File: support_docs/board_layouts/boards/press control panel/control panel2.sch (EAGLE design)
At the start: 21 parts, among them X1 009176002

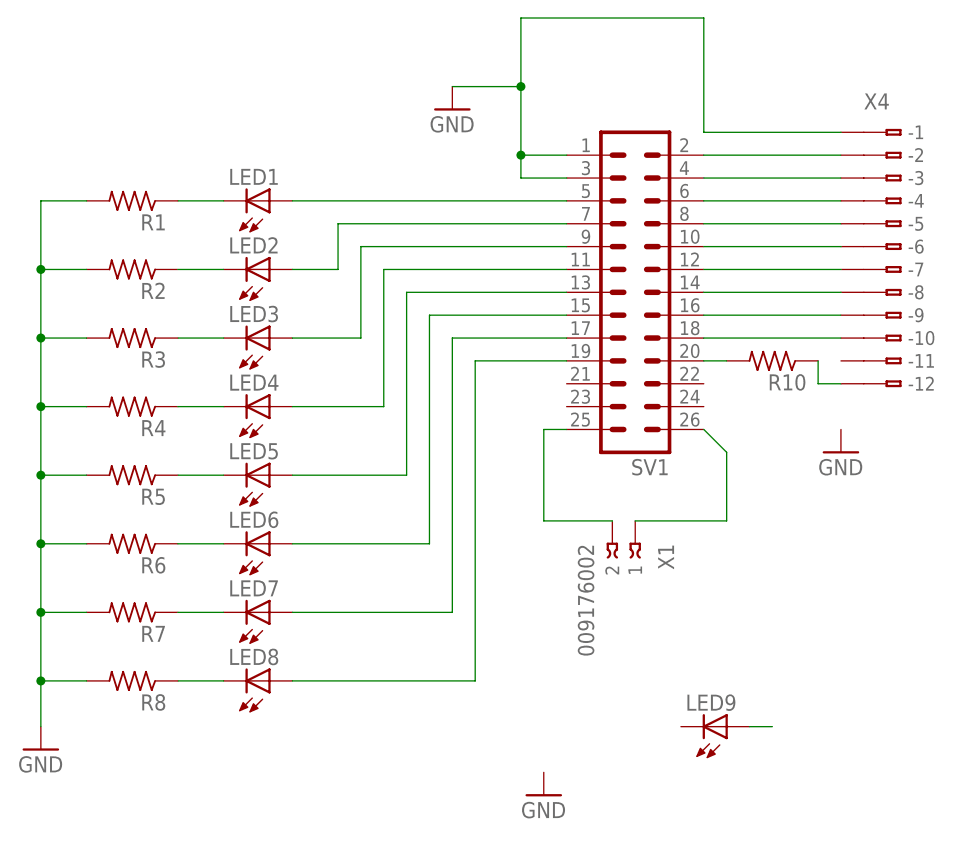
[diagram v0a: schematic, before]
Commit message: add led control
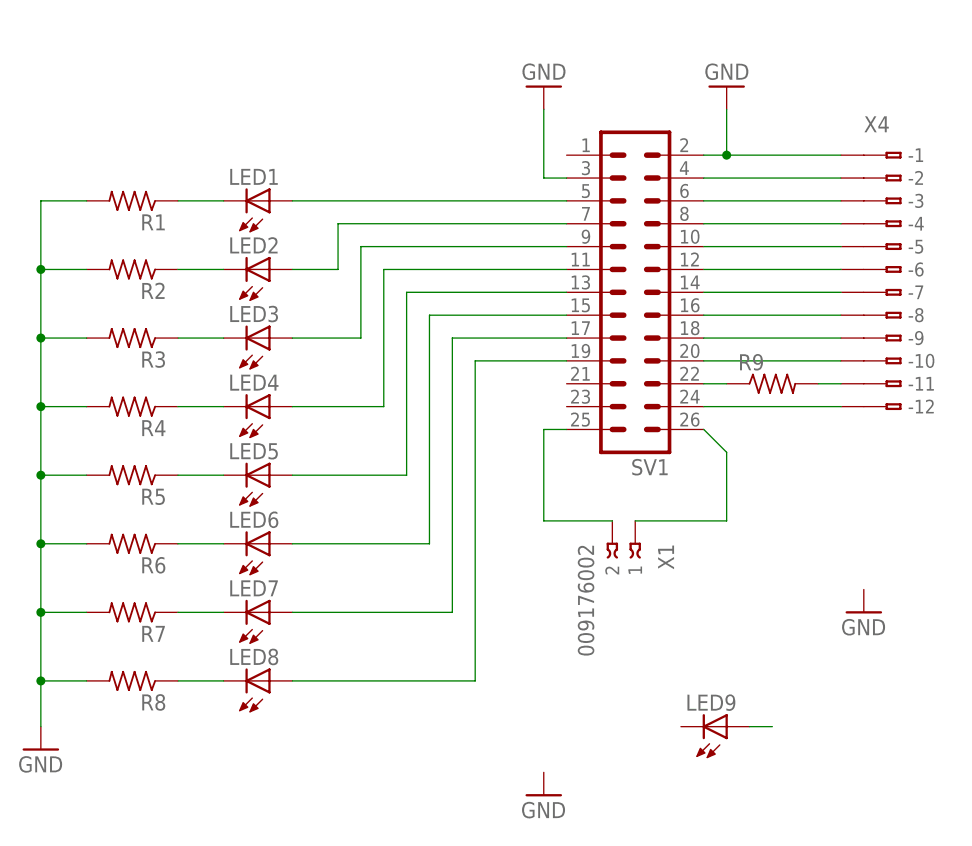
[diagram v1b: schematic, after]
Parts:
- removed R10: (no value), resistor:R-US_0309/V
- added R9: (no value), resistor:R-US_0204/7
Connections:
- new net N$32: R9.2, X4.B-11
- net GND: now also SV1.2; no longer SV1.1
- net N$17: now also SV1.24, X4.B-12; no longer SV1.2, X4.B-2
- net N$18: now also X4.B-2; no longer X4.B-3
- net N$19: now also X4.B-3; no longer X4.B-4
- net N$20: now also X4.B-4; no longer X4.B-5
- net N$21: now also X4.B-5; no longer X4.B-6
- net N$22: now also X4.B-6; no longer X4.B-7
- net N$23: now also X4.B-7; no longer X4.B-8
- net N$24: now also X4.B-8; no longer X4.B-9
- net N$27: now also X4.B-9; no longer X4.B-10
- net N$28: now also X4.B-10; no longer R10.2
- net N$31: now also R9.1, SV1.22; no longer R10.1, X4.B-12
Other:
- moved on the sheet: X4
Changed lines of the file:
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@@
 <?xml version="1.0" encoding="utf-8"?>
 <!DOCTYPE eagle SYSTEM "eagle.dtd">
-<eagle version="8.6.3">
+<eagle version="8.7.0">
 <drawing>
 <settings>
@@
 <part name="X1" library="con-avx" library_urn="urn:adsk.eagle:library:129" deviceset="00917?002" device="6" package3d_urn="urn:adsk.eagle:package:6130/1"/>
 <part name="X4" library="con-wago" library_urn="urn:adsk.eagle:library:197" deviceset="233-212" device=""/>
-<part name="R10" library="resistor" library_urn="urn:adsk.eagle:library:348" deviceset="R-US_" device="0309/V" package3d_urn="urn:adsk.eagle:package:26090/1"/>
+<part name="GND5" library="supply1" library_urn="urn:adsk.eagle:library:371" deviceset="GND" device=""/>
+<part name="R9" library="resistor" library_urn="urn:adsk.eagle:library:348" deviceset="R-US_" device="0204/7" package3d_urn="urn:adsk.eagle:package:25945/1"/>
 </parts>
 <sheets>
@@
 <instance part="LED8" gate="G$1" x="66.04" y="12.7" rot="MR90"/>
 <instance part="GND1" gate="1" x="40.64" y="5.08"/>
-<instance part="GND2" gate="1" x="129.54" y="38.1"/>
+<instance part="GND2" gate="1" x="132.08" y="20.32"/>
 <instance part="LED9" gate="G$1" x="116.84" y="7.62" rot="MR90"/>
 <instance part="GND3" gate="1" x="96.52" y="0"/>
-<instance part="GND4" gate="1" x="86.36" y="76.2"/>
+<instance part="GND4" gate="1" x="96.52" y="78.74" rot="R180"/>
 <instance part="R1" gate="G$1" x="50.8" y="66.04" rot="R180"/>
 <instance part="R2" gate="G$1" x="50.8" y="58.42" rot="R180"/>
@@
 <instance part="R8" gate="G$1" x="50.8" y="12.7" rot="R180"/>
 <instance part="X1" gate="G$1" x="106.68" y="27.94" rot="R270"/>
-<instance part="X4" gate="G$1" x="137.16" y="60.96"/>
-<instance part="R10" gate="G$1" x="121.92" y="48.26" rot="R180"/>
+<instance part="X4" gate="G$1" x="137.16" y="58.42"/>
+<instance part="GND5" gate="1" x="116.84" y="78.74" rot="R180"/>
+<instance part="R9" gate="G$1" x="121.92" y="45.72"/>
 </instances>
 <busses>
@@
 </segment>
 <segment>
+<pinref part="GND5" gate="1" pin="GND"/>
+<wire x1="116.84" y1="76.2" x2="116.84" y2="71.12" width="0.1524" layer="91"/>
+<pinref part="SV1" gate="G$1" pin="2"/>
+<wire x1="116.84" y1="71.12" x2="114.3" y2="71.12" width="0.1524" layer="91"/>
+<pinref part="X4" gate="G$1" pin="B-1"/>
+<wire x1="129.54" y1="71.12" x2="116.84" y2="71.12" width="0.1524" layer="91"/>
+<junction x="116.84" y="71.12"/>
+</segment>
+<segment>
 <pinref part="GND4" gate="1" pin="GND"/>
-<wire x1="86.36" y1="78.74" x2="93.98" y2="78.74" width="0.1524" layer="91"/>
-<wire x1="93.98" y1="78.74" x2="93.98" y2="71.12" width="0.1524" layer="91"/>
+<wire x1="96.52" y1="68.58" x2="96.52" y2="76.2" width="0.1524" layer="91"/>
 <pinref part="SV1" gate="G$1" pin="3"/>
-<wire x1="93.98" y1="71.12" x2="93.98" y2="68.58" width="0.1524" layer="91"/>
-<wire x1="93.98" y1="68.58" x2="99.06" y2="68.58" width="0.1524" layer="91"/>
-<pinref part="SV1" gate="G$1" pin="1"/>
-<wire x1="99.06" y1="71.12" x2="93.98" y2="71.12" width="0.1524" layer="91"/>
-<junction x="93.98" y="71.12"/>
-<wire x1="114.3" y1="86.36" x2="93.98" y2="86.36" width="0.1524" layer="91"/>
-<wire x1="93.98" y1="86.36" x2="93.98" y2="78.74" width="0.1524" layer="91"/>
-<junction x="93.98" y="78.74"/>
-<pinref part="X4" gate="G$1" pin="B-1"/>
-<wire x1="129.54" y1="73.66" x2="114.3" y2="73.66" width="0.1524" layer="91"/>
-<wire x1="114.3" y1="73.66" x2="114.3" y2="86.36" width="0.1524" layer="91"/>
+<wire x1="99.06" y1="68.58" x2="96.52" y2="68.58" width="0.1524" layer="91"/>
 </segment>
 </net>
@@
 </segment>
 </net>
+<net name="N$18" class="0">
+<segment>
+<pinref part="X4" gate="G$1" pin="B-2"/>
+<pinref part="SV1" gate="G$1" pin="4"/>
+<wire x1="129.54" y1="68.58" x2="114.3" y2="68.58" width="0.1524" layer="91"/>
+</segment>
+</net>
+<net name="N$19" class="0">
+<segment>
+<pinref part="X4" gate="G$1" pin="B-3"/>
+<pinref part="SV1" gate="G$1" pin="6"/>
+<wire x1="129.54" y1="66.04" x2="114.3" y2="66.04" width="0.1524" layer="91"/>
+</segment>
+</net>
+<net name="N$20" class="0">
+<segment>
+<pinref part="X4" gate="G$1" pin="B-4"/>
+<pinref part="SV1" gate="G$1" pin="8"/>
+<wire x1="129.54" y1="63.5" x2="114.3" y2="63.5" width="0.1524" layer="91"/>
+</segment>
+</net>
+<net name="N$21" class="0">
+<segment>
+<pinref part="X4" gate="G$1" pin="B-5"/>
+<pinref part="SV1" gate="G$1" pin="10"/>
+<wire x1="129.54" y1="60.96" x2="114.3" y2="60.96" width="0.1524" layer="91"/>
+</segment>
+</net>
+<net name="N$22" class="0">
+<segment>
+<pinref part="X4" gate="G$1" pin="B-6"/>
+<pinref part="SV1" gate="G$1" pin="12"/>
+<wire x1="129.54" y1="58.42" x2="114.3" y2="58.42" width="0.1524" layer="91"/>
+</segment>
+</net>
+<net name="N$23" class="0">
+<segment>
+<pinref part="X4" gate="G$1" pin="B-7"/>
+<pinref part="SV1" gate="G$1" pin="14"/>
+<wire x1="129.54" y1="55.88" x2="114.3" y2="55.88" width="0.1524" layer="91"/>
+</segment>
+</net>
+<net name="N$24" class="0">
+<segment>
+<pinref part="X4" gate="G$1" pin="B-8"/>
+<pinref part="SV1" gate="G$1" pin="16"/>
+<wire x1="129.54" y1="53.34" x2="114.3" y2="53.34" width="0.1524" layer="91"/>
+</segment>
+</net>
+<net name="N$27" class="0">
+<segment>
+<pinref part="X4" gate="G$1" pin="B-9"/>
+<pinref part="SV1" gate="G$1" pin="18"/>
+<wire x1="129.54" y1="50.8" x2="114.3" y2="50.8" width="0.1524" layer="91"/>
+</segment>
+</net>
+<net name="N$28" class="0">
+<segment>
+<pinref part="X4" gate="G$1" pin="B-10"/>
+<pinref part="SV1" gate="G$1" pin="20"/>
+<wire x1="129.54" y1="48.26" x2="114.3" y2="48.26" width="0.1524" layer="91"/>
+</segment>
+</net>
+<net name="N$31" class="0">
+<segment>
+<pinref part="SV1" gate="G$1" pin="22"/>
+<wire x1="114.3" y1="45.72" x2="116.84" y2="45.72" width="0.1524" layer="91"/>
+<pinref part="R9" gate="G$1" pin="1"/>
+</segment>
+</net>
+<net name="N$32" class="0">
+<segment>
+<pinref part="X4" gate="G$1" pin="B-11"/>
+<wire x1="127" y1="45.72" x2="129.54" y2="45.72" width="0.1524" layer="91"/>
+<pinref part="R9" gate="G$1" pin="2"/>
+</segment>
+</net>
 <net name="N$17" class="0">
 <segment>
-<pinref part="SV1" gate="G$1" pin="2"/>
-<pinref part="X4" gate="G$1" pin="B-2"/>
-<wire x1="114.3" y1="71.12" x2="129.54" y2="71.12" width="0.1524" layer="91"/>
-</segment>
-</net>
-<net name="N$18" class="0">
-<segment>
-<pinref part="SV1" gate="G$1" pin="4"/>
-<pinref part="X4" gate="G$1" pin="B-3"/>
-<wire x1="114.3" y1="68.58" x2="129.54" y2="68.58" width="0.1524" layer="91"/>
-</segment>
-</net>
-<net name="N$19" class="0">
-<segment>
-<pinref part="SV1" gate="G$1" pin="6"/>
-<pinref part="X4" gate="G$1" pin="B-4"/>
-<wire x1="114.3" y1="66.04" x2="129.54" y2="66.04" width="0.1524" layer="91"/>
-</segment>
-</net>
-<net name="N$20" class="0">
-<segment>
-<pinref part="SV1" gate="G$1" pin="8"/>
-<pinref part="X4" gate="G$1" pin="B-5"/>
-<wire x1="114.3" y1="63.5" x2="129.54" y2="63.5" width="0.1524" layer="91"/>
-</segment>
-</net>
-<net name="N$21" class="0">
-<segment>
-<pinref part="SV1" gate="G$1" pin="10"/>
-<pinref part="X4" gate="G$1" pin="B-6"/>
-<wire x1="114.3" y1="60.96" x2="129.54" y2="60.96" width="0.1524" layer="91"/>
-</segment>
-</net>
-<net name="N$22" class="0">
-<segment>
-<pinref part="SV1" gate="G$1" pin="12"/>
-<pinref part="X4" gate="G$1" pin="B-7"/>
-<wire x1="114.3" y1="58.42" x2="129.54" y2="58.42" width="0.1524" layer="91"/>
-</segment>
-</net>
-<net name="N$23" class="0">
-<segment>
-<pinref part="SV1" gate="G$1" pin="14"/>
-<pinref part="X4" gate="G$1" pin="B-8"/>
-<wire x1="114.3" y1="55.88" x2="129.54" y2="55.88" width="0.1524" layer="91"/>
-</segment>
-</net>
-<net name="N$24" class="0">
-<segment>
-<pinref part="SV1" gate="G$1" pin="16"/>
-<pinref part="X4" gate="G$1" pin="B-9"/>
-<wire x1="114.3" y1="53.34" x2="129.54" y2="53.34" width="0.1524" layer="91"/>
-</segment>
-</net>
-<net name="N$27" class="0">
-<segment>
-<pinref part="SV1" gate="G$1" pin="18"/>
-<pinref part="X4" gate="G$1" pin="B-10"/>
-<wire x1="114.3" y1="50.8" x2="129.54" y2="50.8" width="0.1524" layer="91"/>
-</segment>
-</net>
-<net name="N$28" class="0">
-<segment>
-<pinref part="SV1" gate="G$1" pin="20"/>
-<wire x1="114.3" y1="48.26" x2="116.84" y2="48.26" width="0.1524" layer="91"/>
-<pinref part="R10" gate="G$1" pin="2"/>
-</segment>
-</net>
-<net name="N$31" class="0">
-<segment>
-<pinref part="R10" gate="G$1" pin="1"/>
-<wire x1="127" y1="48.26" x2="127" y2="45.72" width="0.1524" layer="91"/>
+<pinref part="SV1" gate="G$1" pin="24"/>
 <pinref part="X4" gate="G$1" pin="B-12"/>
-<wire x1="127" y1="45.72" x2="129.54" y2="45.72" width="0.1524" layer="91"/>
-</segment>
-</net>
+<wire x1="114.3" y1="43.18" x2="129.54" y2="43.18" width="0.1524" layer="91"/>
+</segment>
+</net>
